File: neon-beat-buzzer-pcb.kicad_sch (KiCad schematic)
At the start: 0 parts

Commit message: Add main features for the PCB Still missing: - battery measure - charging LED
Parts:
- added C1: 4.7uF, symbol Device:C
- added C2, C3: 1uF, symbol Device:C
- added C4, C5, C6: 10uF, symbol Device:C
- added D1, D2: D, symbol Device:D
- added D3, D4: WS2812B, LED_SMD:LED_WS2812B_PLCC4_5.0x5.0mm_P3.2mm, symbol LED:WS2812B
- added J2: BATT, symbol Connector:Conn_01x02_Pin
- added J3: SWITCH_CON, symbol Connector:Conn_01x02_Pin
- added J4: BUZZER_CON, symbol Connector:Conn_01x02_Pin
- added J4: USB_C_Receptacle_USB2.0_14P, symbol Connector:USB_C_Receptacle_USB2.0_14P
- added L1: 2.2uH, symbol Device:L
- added R1, R2: 5.1k, symbol Device:R
- added R3, R4: 22, symbol Device:R
- added R5: R, symbol Device:R
- added R6: 2.8k, symbol Device:R
- added R7: 3.3k, symbol Device:R
- added R8: 2k, symbol Device:R
- added R9: 10k, symbol Device:R
- added U1: ESP32-C3-MINI-1, PCM_Espressif:ESP32-C3-MINI-1, symbol PCM_Espressif:ESP32-C3-MINI-1
- added U2: BQ24074RGT, Package_DFN_QFN:VQFN-16-1EP_3x3mm_P0.5mm_EP1.6x1.6mm, symbol Battery_Management:BQ24074RGT
- added U3: TPS22929D, Package_TO_SOT_SMD:SOT-23-6, symbol Power_Management:TPS22929D
- added U4: MCP1700x-330xxTT, Package_TO_SOT_SMD:SOT-23, symbol Regulator_Linear:MCP1700x-330xxTT
- added U5: TPS610997DRV, Package_SON:WSON-6-1EP_2x2mm_P0.65mm_EP1x1.6mm, symbol Regulator_Switching:TPS610997DRV
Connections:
- new net: J4.A6 (D+), J4.B6 (D+), R4.1
- new net: R5.2, U2.1 (TS)
- new net: R7.1, U2.12 (ILIM)
- new net: R8.1, U2.15 (ITERM)
- new net: R6.2, U2.16 (ISET)
- new net: D1.1 (K), D2.1 (K), U3.3 (ON)
- new net: C3.1, R9.2, U1.8 (EN/CHIP_PU)
- new net: L1.2, U5.5 (SW)
- new net: J4.B5 (CC2), R2.1
- new net: J4.A5 (CC1), R1.1
- new net: D3.2 (DOUT), D4.4 (DIN)
- new net: J4.A7 (D-), J4.B7 (D-), R3.1
- new net GND: C1.2, C2.2, C3.2, C4.2, C5.2, C6.2, D3.3 (VSS), D4.3 (VSS), J2.2 (Pin_2), J4.A1 (GND), J4.A12 (GND), J4.B1 (GND), J4.B12 (GND), J4.SH (SHIELD), R1.2, R2.2, R5.1, R6.1, R7.2, R8.2, U1.1 (GND), U1.11 (GND), U1.14 (GND), U1.2 (GND), U1.36 (GND), U1.37 (GND), U1.38 (GND), U1.39 (GND), U1.40 (GND), U1.41 (GND), U1.42 (GND), U1.43 (GND), U1.44 (GND), U1.45 (GND), U1.46 (GND), U1.47 (GND), U1.48 (GND), U1.49 (GND), U1.50 (GND), U1.51 (GND), U1.52 (GND), U1.53 (GND), U2.14 (TMR), U2.17 (VSS), U2.4 (~{CE}), U2.5 (EN2), U2.8 (VSS), U3.2 (GND), U3.5 (GND), U4.1 (GND), U5.1 (GND), U5.3 (FB), U5.7 (GND)
- new net buzzer: J4.2 (Pin_2), U1.6 (GPIO3/ADC1_CH3)
- new net esp_usb_dm: R4.2, U1.26 (GPIO18/USB_D-)
- new net esp_usb_dp: R3.2, U1.27 (GPIO19/USB_D+)
- new net led_in: D3.4 (DIN), U1.5 (GPIO2/ADC1_CH2)
- new net switch_a: J3.1 (Pin_1), U2.10 (OUT), U2.11 (OUT), U3.4 (VIN), U3.6 (VIN)
- new net switch_b: D1.2 (A), J3.2 (Pin_2)
- new net v_3v3: C4.1, J4.1 (Pin_1), L1.1, R9.1, U1.3 (3V3), U4.2 (VO), U5.4 (EN), U5.6 (VI)
- new net v_5v: C5.1, C6.1, D3.1 (VDD), D4.1 (VDD), U5.2 (VOUT)
- new net v_batt: C1.1, J2.1 (Pin_1), U2.2 (BAT), U2.3 (BAT)
- new net v_ldo: U3.1 (VOUT), U4.3 (VI)
- new net v_usb: C2.1, D2.2 (A), J4.A4 (VBUS), J4.A9 (VBUS), J4.B4 (VBUS), J4.B9 (VBUS), U2.13 (IN), U2.6 (EN1)
- no-connect marks 0 -> 12
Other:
- company: (none) -> Neon Beat
- title: (none) -> Neon Beat Buzzer PCB

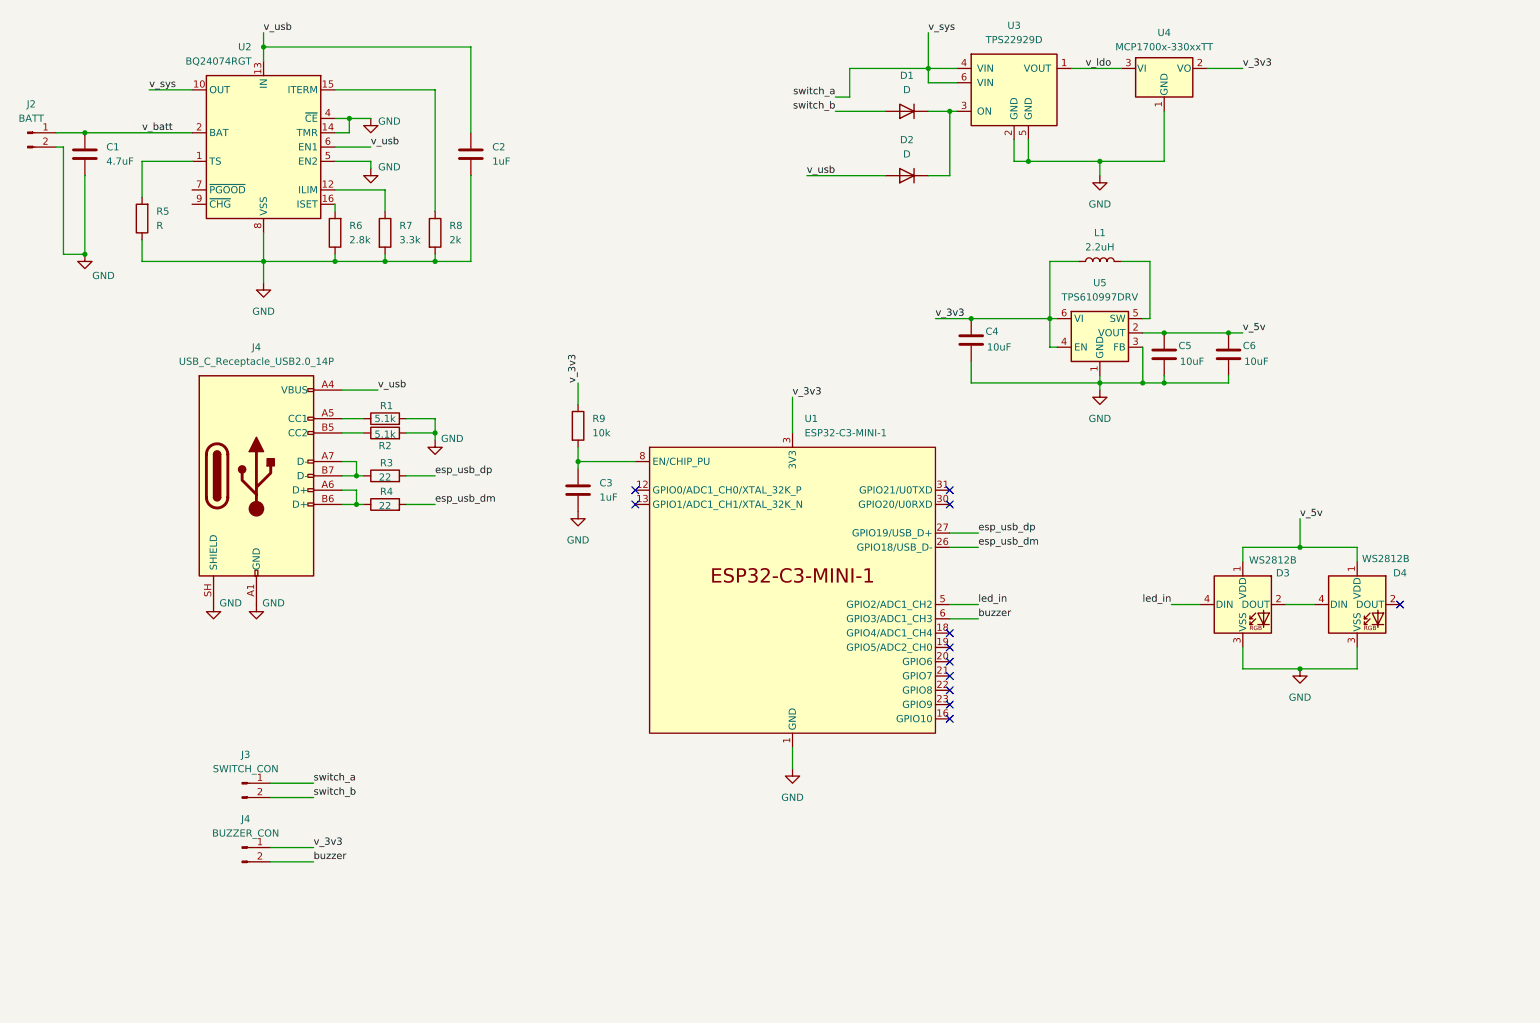
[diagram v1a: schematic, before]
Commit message: schematic: all main features are now on-board
Signed-off-by: Alexis Lothoré <alexis.lothore@gmail.com>
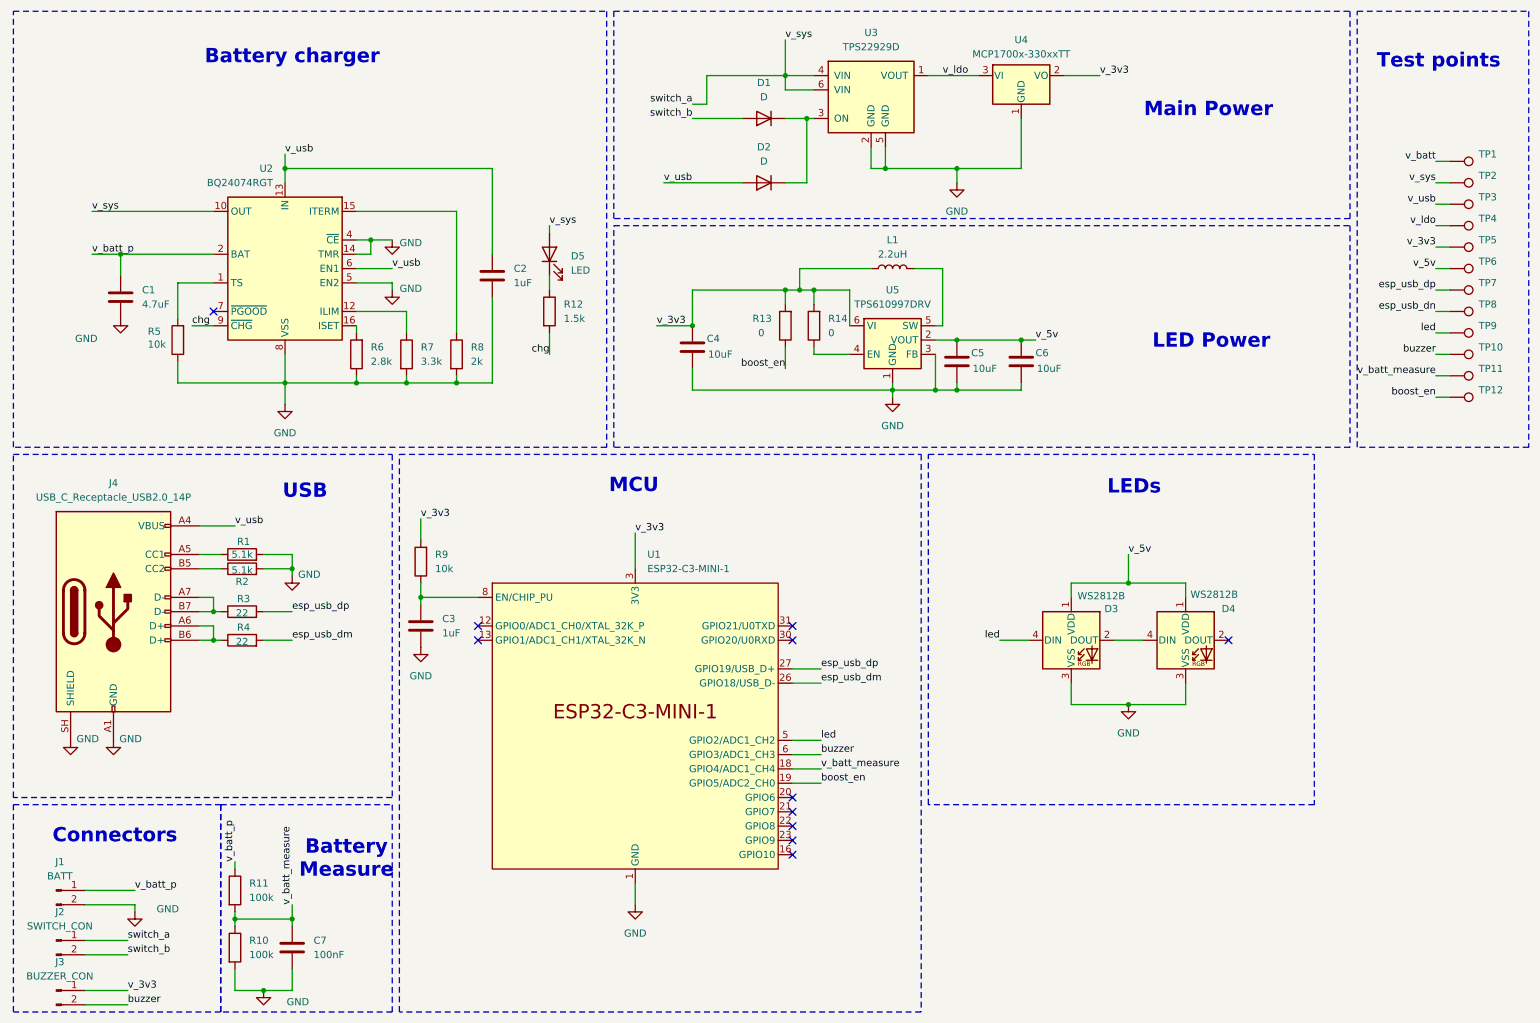
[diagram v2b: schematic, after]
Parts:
- removed J2: BATT, symbol Connector:Conn_01x02_Pin
- added C7: 100nF, symbol Device:C
- added D5: LED, symbol Device:LED
- added J1: BATT, symbol Connector:Conn_01x02_Pin
- added R10, R11: 100k, symbol Device:R
- added R12: 1.5k, symbol Device:R
- added R13, R14: 0, symbol Device:R
- added TP1, TP10, TP11, TP12, TP2, TP3, TP4, TP5, TP6, TP7, TP8, TP9: (no value), symbol Connector:TestPoint
- R5: value R -> 10k
- renumbered J3 to J2, J4 to J3
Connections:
- net GND: now also C7.2, J1.2 (Pin_2), R10.2
- net buzzer: now also TP10.1
- net esp_usb_dp: now also TP7.1
- net switch_a: now also D5.2 (A), TP2.1
- net v_3v3: now also R9.2, R13.2, R14.2, TP5.1; no longer R9.1, U5.4 (EN)
- net v_5v: now also TP6.1
- net v_batt: now also TP1.1; no longer C1.1, U2.2 (BAT), U2.3 (BAT)
- net v_ldo: now also TP4.1
- net v_usb: now also TP3.1
- net chg: now reaches U2.9 (~{CHG})
- net chg: now also R12.2
- net v_batt_measure: now reaches U1.18 (GPIO4/ADC1_CH4)
- net v_batt_measure: now also C7.1, R10.1, R11.2, TP11.1
- net boost_en: now reaches U1.19 (GPIO5/ADC2_CH0)
- net boost_en: now also R13.1, TP12.1
- net at C3.1, U1.8 (EN/CHIP_PU): now also R9.1; no longer R9.2
- net led_in renamed led
- net led: now also TP9.1
- new net: D5.1 (K), R12.1
- new net: R14.1, U5.4 (EN)
- new net esp_usb_dn: TP8.1
- new net v_batt_p: C1.1, J1.1 (Pin_1), R11.1, U2.2 (BAT), U2.3 (BAT)
- no-connect marks 12 -> 11
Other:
- note added: "Battery Measure"
- note added: "Battery charger"
- note added: "Connectors"
- note added: "LED Power"
- note added: "LEDs"
- note added: "MCU"
- note added: "Main Power"
- note added: "Test points"
- note added: "USB"
- moved on the sheet: C1, C2, C3, C4, C5, C6, D1, D2, D3, D4, J2, J3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

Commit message: schematic: fix a handful of issues
- invert usb signals
- set power supply on power input pins
- adjust battery measure divider to fit 1.1v ADC full scale
- add decoupling capacitors on MCU

Signed-off-by: Alexis Lothoré <alexis.lothore@gmail.com>
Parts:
- added C8: 0.1uF, symbol Device:C
- added C9: 10uF, symbol Device:C
- R11: value 100k -> 240k
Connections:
- net esp_usb_dn is gone; now on net esp_usb_dm: TP8.1
- net v_batt is gone; now on net v_batt_p: TP1.1
- net GND: now also C8.2, C9.2
- net esp_usb_dm: now also R3.2; no longer R4.2
- net esp_usb_dp: now also R4.2; no longer R3.2
- net v_3v3: now also C8.1, C9.1
- net buzzer renamed button
- net switch_a renamed v_sys
- net switch_b renamed switch
- net v_batt_measure renamed v_batt_meas

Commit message: schematic: add esd protection, and add all footprints
Signed-off-by: Alexis Lothoré <alexis.lothore@bootlin.com>
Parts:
- added C10: 100nF, Capacitor_SMD:C_1206_3216Metric, symbol Device:C
- added D6: SMF5V0A, Diode_SMD:D_SMF, symbol Diode:SMF5V0A
- added U6: USBLC6-2SC6, Package_TO_SOT_SMD:SOT-23-6, symbol Power_Protection:USBLC6-2SC6
- C1, C2, C3, C4, C5, C6, C7, C8, C9: footprint (none) -> Capacitor_SMD:C_1206_3216Metric
- D1, D2, D5: footprint (none) -> Diode_SMD:D_1206_3216Metric
- J1, J2, J3: footprint (none) -> Connector_Molex:Molex_PicoBlade_53048-0210_1x02_P1.25mm_Horizontal
- J4: footprint (none) -> Connector_USB:USB_C_Receptacle_GCT_USB4110
- L1: footprint (none) -> Inductor_SMD:L_APV_ANR252010
- R1, R10, R11, R12, R13, R14, R2, R3, R4, R5, R6, R7, R8, R9: footprint (none) -> Resistor_SMD:R_1206_3216Metric
- TP1, TP10, TP11, TP12, TP2, TP3, TP4, TP5, TP6, TP7, TP8, TP9: footprint (none) -> TestPoint:TestPoint_Pad_D2.0mm
- U1: footprint PCM_Espressif:ESP32-C3-MINI-1 -> PCM_Espressif:ESP32-C3-MINI-1U
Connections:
- net GND: now also C10.2, D6.2 (A2), U6.2 (GND)
- net esp_usb_dm: now also R4.2; no longer R3.2
- net esp_usb_dp: now also R3.2; no longer R4.2
- net v_usb: now also C10.1, D6.1 (A1), U6.5 (VBUS)
- net at J4.A6 (D+), J4.B6 (D+): now also U6.3 (I/O2); no longer R4.1
- net at J4.A7 (D-), J4.B7 (D-): now also U6.1 (I/O1); no longer R3.1
- new net: R3.1, U6.4 (I/O2)
- new net: R4.1, U6.6 (I/O1)
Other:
- moved on the sheet: J4, R1, R2

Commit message: pcb: move all composents in proper place
Signed-off-by: Alexis Lothoré <alexis.lothore@gmail.com>
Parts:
- removed J4: USB_C_Receptacle_USB2.0_14P, Connector_USB:USB_C_Receptacle_GCT_USB4110, symbol Connector:USB_C_Receptacle_USB2.0_14P
- added C11, C14: 1uF, Capacitor_SMD:C_0805_2012Metric_Pad1.18x1.45mm_HandSolder, symbol Device:C
- added C12, C13: 0.1uF, Capacitor_SMD:C_0805_2012Metric_Pad1.18x1.45mm_HandSolder, symbol Device:C
- added J4: USB_C_Receptacle_USB2.0_16P, Connector_USB:USB_C_Receptacle_GCT_USB4105-xx-A_16P_TopMnt_Horizontal, symbol Connector:USB_C_Receptacle_USB2.0_16P
- added R15: 0, Resistor_SMD:R_0805_2012Metric_Pad1.20x1.40mm_HandSolder, symbol Device:R
- C1, C10, C2, C3, C4, C5, C6, C7, C8, C9: footprint Capacitor_SMD:C_1206_3216Metric -> Capacitor_SMD:C_0805_2012Metric_Pad1.18x1.45mm_HandSolder
- D1, D2, D5: footprint Diode_SMD:D_1206_3216Metric -> Diode_SMD:D_0805_2012Metric_Pad1.15x1.40mm_HandSolder
- J1: value BATT -> BATT_CON
- J3: value BUZZER_CON -> BUTTON_CON
- R1, R10, R11, R12, R13, R2, R3, R4, R5, R6, R7, R8, R9: footprint Resistor_SMD:R_1206_3216Metric -> Resistor_SMD:R_0805_2012Metric_Pad1.20x1.40mm_HandSolder
- R14: footprint Resistor_SMD:R_1206_3216Metric -> Resistor_SMD:R_0805_2012Metric_Pad1.20x1.40mm_HandSolder; now not fitted
- TP1, TP10, TP11, TP12, TP2, TP3, TP4, TP5, TP6, TP7, TP8, TP9: footprint TestPoint:TestPoint_Pad_D2.0mm -> TestPoint:TestPoint_Pad_D1.0mm
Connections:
- net GND: now also C11.2, C12.2, C13.2, C14.2, J4.A1 (GND), J4.A12 (GND), J4.B1 (GND), J4.B12 (GND), J4.SH (SHIELD)
- net v_3v3: now also C13.1
- net v_batt_p: now also R15.2; no longer J1.1 (Pin_1)
- net v_ldo: now also C12.1, C14.1
- net v_sys: now also C11.1
- net v_usb: now also J4.A4 (VBUS), J4.A9 (VBUS), J4.B4 (VBUS), J4.B9 (VBUS)
- net at U6.1 (I/O1): now also J4.A7 (D-), J4.B7 (D-)
- net at U6.3 (I/O2): now also J4.A6 (D+), J4.B6 (D+)
- net at R2.1: now also J4.B5 (CC2)
- net at R1.1: now also J4.A5 (CC1)
- new net: J1.1 (Pin_1), R15.1
- no-connect marks 11 -> 13
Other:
- moved on the sheet: D1, D2, D6, U4

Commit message: schematic: fix multiple points
- use a LDO with lower drop
- feed the boost directly with v_sys
- add a few caps around WS2812 leds
- fix mistake on the boost enable pin

Signed-off-by: Alexis Lothoré <alexis.lothore@gmail.com>
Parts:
- removed U4: MCP1700x-330xxTT, Package_TO_SOT_SMD:SOT-23, symbol Regulator_Linear:MCP1700x-330xxTT
- added C15, C16: 0.1uF, symbol Device:C
- added R16: 10k, symbol Device:R
- added U4: 74AHCT1G125, symbol 74xGxx:74AHCT1G125
- added U7: XC6210B332MR, Package_TO_SOT_SMD:SOT-23-5, symbol Regulator_Linear:XC6210B332MR
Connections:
- net GND: now also C15.2, C16.2, R16.2, U4.1, U4.3 (GND), U7.2 (GND)
- net boost_en: now also R16.1
- net led: now also U4.2; no longer D3.4 (DIN)
- net v_3v3: now also U7.5 (VOUT); no longer C4.1, L1.1, R13.2, R14.2, U5.6 (VI)
- net v_5v: now also C15.1, C16.1, U4.5 (VCC)
- net v_ldo: now also U7.1 (VIN), U7.3 (CE)
- net v_sys: now also C4.1, L1.1, R14.2, U5.6 (VI)
- net at R14.1, U5.4 (EN): now also R13.2
- new net: D3.4 (DIN), U4.4
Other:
- moved on the sheet: C13, C14, C4, D3, D4, R13
